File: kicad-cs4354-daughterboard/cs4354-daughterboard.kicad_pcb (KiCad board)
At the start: 2 copper layers, 20 parts, among them J1 DAC1_pin1to7, J2 DAC2_pin1to7, J3 DAC1_pin8to14, J4 DAC2_pin8to14, J5 Conn_01x02_Male, J6 Conn_01x02_Male, J7 I2S3_MCK, J8 I2S3_WS, J9 +3.3V, U1 CS4354DAC

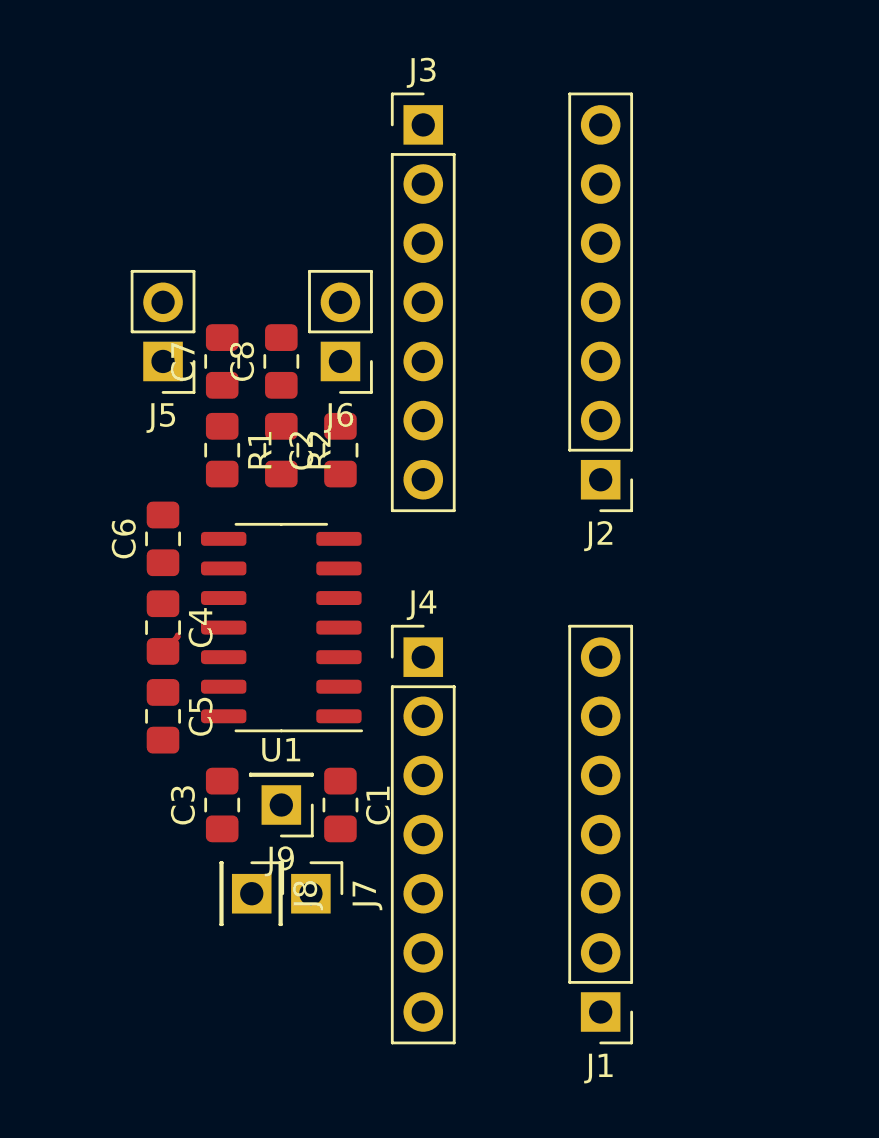
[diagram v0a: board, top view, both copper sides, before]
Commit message: renamed kicad daughterboard 'noDIL'
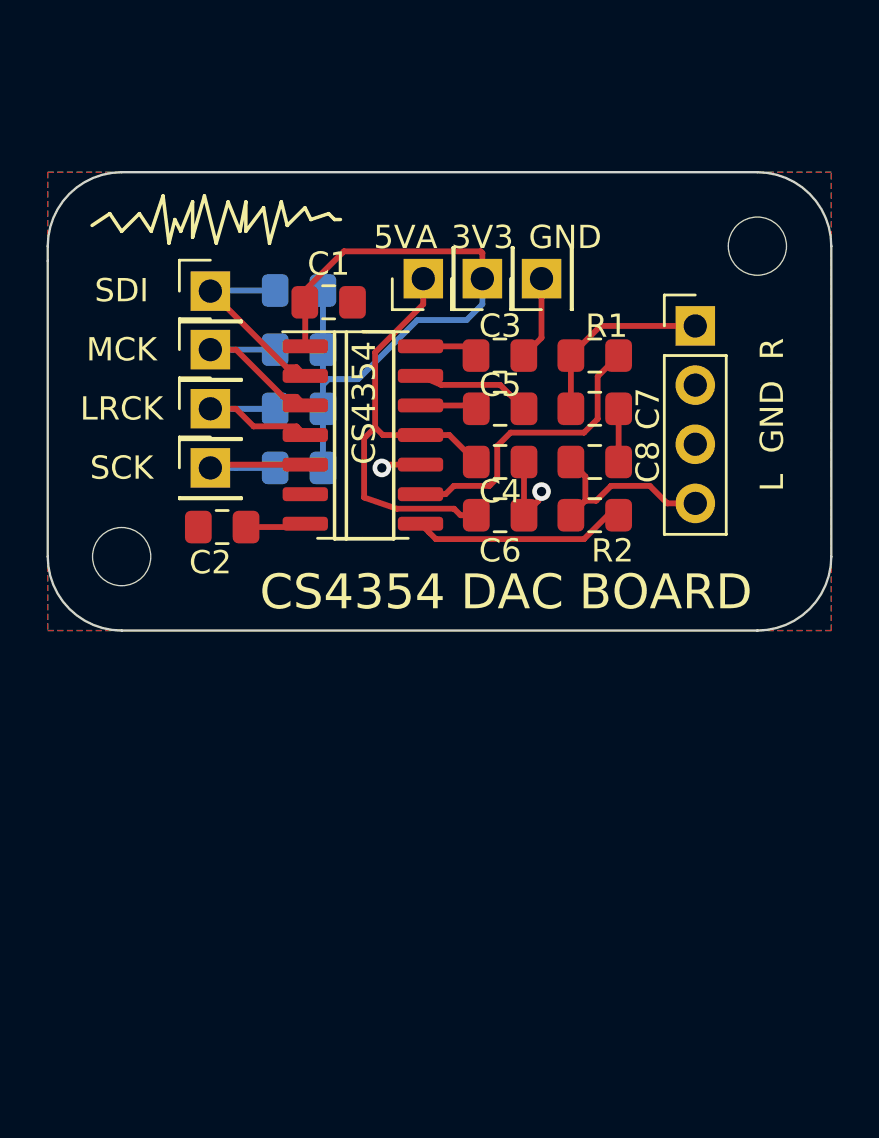
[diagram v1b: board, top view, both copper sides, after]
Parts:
- removed J1: DAC1_pin1to7, Connector_PinHeader_2.54mm:PinHeader_1x07_P2.54mm_Vertical
- removed J2: DAC2_pin1to7, Connector_PinHeader_2.54mm:PinHeader_1x07_P2.54mm_Vertical
- removed J3: DAC1_pin8to14, Connector_PinHeader_2.54mm:PinHeader_1x07_P2.54mm_Vertical
- removed J4: DAC2_pin8to14, Connector_PinHeader_2.54mm:PinHeader_1x07_P2.54mm_Vertical
- removed J5, J6: Conn_01x02_Male, Connector_PinHeader_2.54mm:PinHeader_1x02_P2.54mm_Vertical
- removed J7: I2S3_MCK, Connector_PinHeader_2.54mm:PinHeader_1x01_P2.54mm_Vertical
- removed J9: +3.3V, Connector_PinHeader_2.54mm:PinHeader_1x01_P2.54mm_Vertical
- added 3V3: 3V3, Connector_PinHeader_2.54mm:PinHeader_1x01_P2.54mm_Vertical, F.Cu at (139.7, 59.9)
- added B_GND_A1: L GND R, Connector_PinHeader_2.54mm:PinHeader_1x04_P2.54mm_Vertical, F.Cu at (148.8, 62.0)
- added GND1: GND, Connector_PinHeader_2.54mm:PinHeader_1x01_P2.54mm_Vertical, F.Cu at (142.2, 59.9)
- added H1: MountingHole, MountingHole:MountingHole_2.5mm, F.Cu at (124.2, 71.9)
- added H2: MountingHole, MountingHole:MountingHole_2.5mm, F.Cu at (151.5, 58.5)
- added LRCK1: LRCK, Connector_PinHeader_2.54mm:PinHeader_1x01_P2.54mm_Vertical, F.Cu at (128.0, 65.5)
- added MCK1: MCK, Connector_PinHeader_2.54mm:PinHeader_1x01_P2.54mm_Vertical, F.Cu at (128.0, 63.0)
- added R3: DNP, Resistor_SMD:R_0805_2012Metric_Pad1.15x1.40mm_HandSolder, B.Cu at (131.8, 60.5)
- added R4: DNP, Resistor_SMD:R_0805_2012Metric_Pad1.15x1.40mm_HandSolder, B.Cu at (131.8, 63.0)
- added R5: DNP, Resistor_SMD:R_0805_2012Metric_Pad1.15x1.40mm_HandSolder, B.Cu at (131.8, 65.5)
- added R6: DNP, Resistor_SMD:R_0805_2012Metric_Pad1.15x1.40mm_HandSolder, B.Cu at (131.8, 68.1)
- added SCK1: SCK, Connector_PinHeader_2.54mm:PinHeader_1x01_P2.54mm_Vertical, F.Cu at (128.0, 68.1)
- added SDI1: SDI, Connector_PinHeader_2.54mm:PinHeader_1x01_P2.54mm_Vertical, F.Cu at (128.0, 60.5)
- J8: value I2S3_WS -> 5VA
- U1: value CS4354DAC -> CS4354
- moved J8 27.4 mm to (137.2, 59.9), turned to 90 degrees
- moved C3 22.7 mm to (140.5, 63.2), turned to 180 degrees
- moved C1 21.6 mm to (133.1, 61.0), turned to 0 degrees
- moved C5 19.6 mm to (140.5, 65.5), turned to 0 degrees
- moved R1 16.5 mm to (144.5, 63.2), turned to 0 degrees
- moved C7 16.1 mm to (144.5, 65.5), turned to 0 degrees
- moved C4 16.1 mm to (140.5, 67.8), turned to 0 degrees
- moved C6 14.5 mm to (140.5, 70.1), turned to 0 degrees
- moved C8 14.1 mm to (144.5, 67.8), turned to 0 degrees
- moved R2 13.7 mm to (144.5, 70.1), turned to 0 degrees
- moved U1 8.98 mm to (134.6, 66.7), turned to 0 degrees
- moved C2 6.06 mm to (128.5, 70.6), turned to 180 degrees
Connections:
- J8 pad 1: Net-(J8-Pad1) -> +5VA
- U1 pad 2: /SPI_MO -> Net-(R3-Pad1)
- U1 pad 4: Net-(J8-Pad1) -> Net-(LRCK1-Pad1)
- U1 pad 5: /SPI_CK -> Net-(R6-Pad1)
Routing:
- net +3V3: track 0.00 -> 28.9 mm
- net +5VA: track 0.00 -> 20.4 mm
- net Net-(R1-Pad2): track 0.00 -> 12.8 mm
- net GND: track 0.95 -> 11.2 mm, vias 0 -> 2
- net Net-(R2-Pad2): track 0.00 -> 9.21 mm
- net Net-(R3-Pad1): track 0.00 -> 8.38 mm
- net /2_VOUT_A(to1.8K): track 0.00 -> 8.16 mm
- net /1_VOUT_A(to1.8K): track 0.00 -> 8.10 mm
- net Net-(MCK1-Pad1): track 0.00 -> 7.85 mm
- net Net-(LRCK1-Pad1): track 0.00 -> 7.33 mm
- net Net-(R6-Pad1): track 0.00 -> 7.27 mm
- net Net-(C5-Pad2): track 0.00 -> 4.95 mm
- net Net-(C2-Pad1): track 0.00 -> 2.60 mm
- net Net-(C3-Pad2): track 0.00 -> 2.55 mm
- net Net-(C5-Pad1): track 0.00 -> 2.45 mm
- added copper zone on B.Cu, net GND
- added copper zone on F.Cu, net GND
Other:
- board outline added: 33.7 x 19.7 mm
- rule pad_to_mask_clearance: 0.051 -> 0
- board text added: "CS4354 DAC BOARD"
